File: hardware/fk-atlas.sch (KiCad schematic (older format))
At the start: 50 parts, among them J1 CONN-HDR-2x5, J2 MICRO-USB, J3 Conn_01x02, J4 Conn_01x09, Q1 2N7002LT1G, Q2 2N7002LT1G, Q3 2N7002LT1G, Q4 2N7002LT1G, Q5 2N7002LT1G, SW1 SPNO, U1 S25FL1xxK0XM, U2 ATSAMD21G18A-AU, U3 MCP1700T-3302E/MB, Y1 FC-135

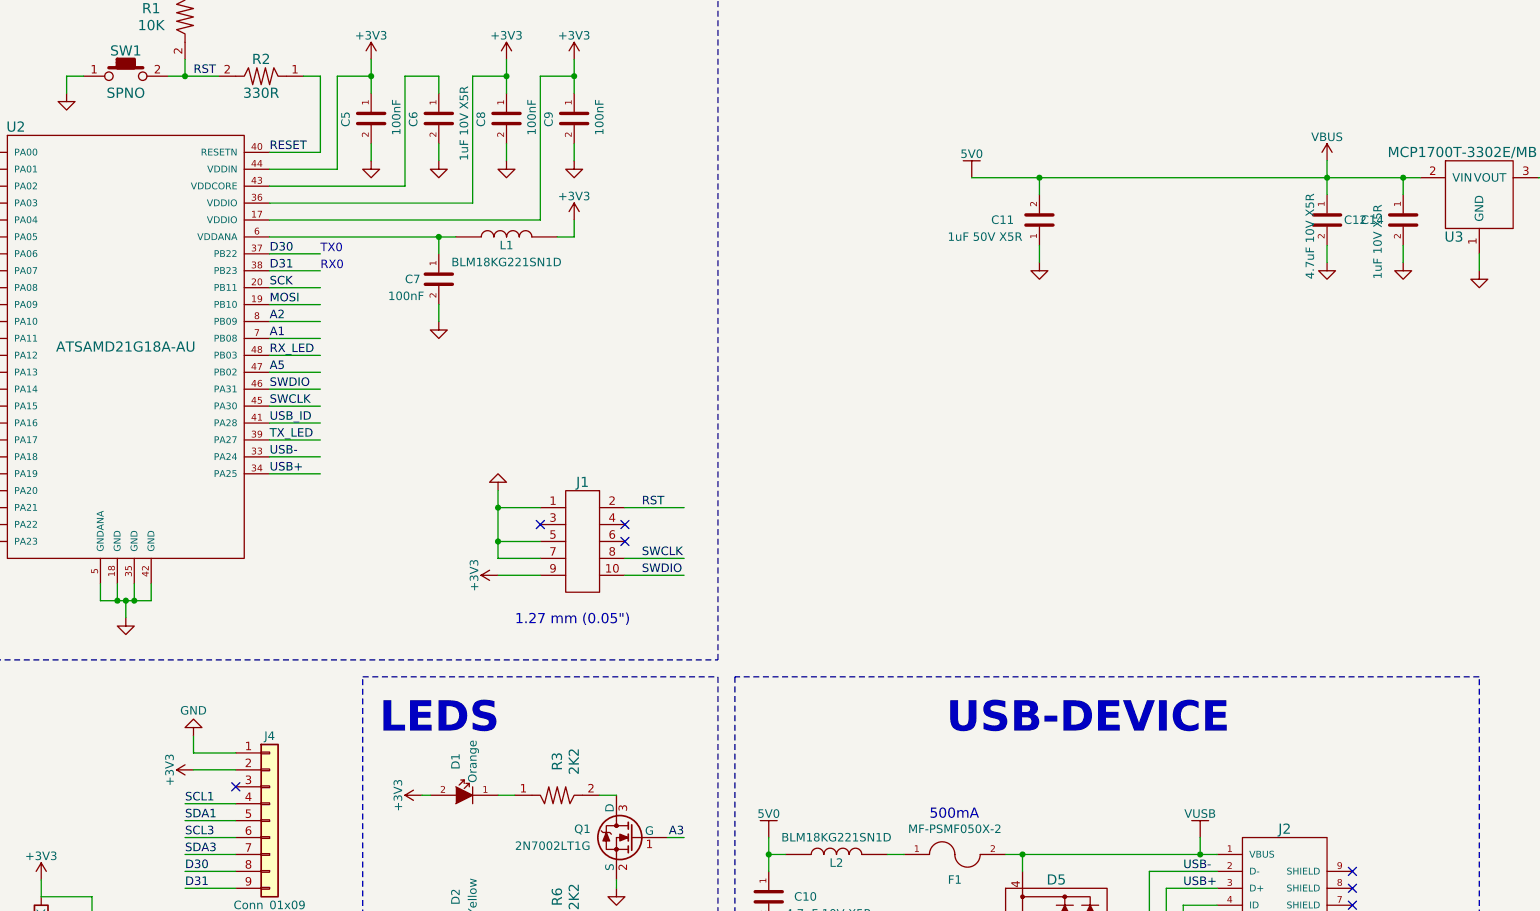
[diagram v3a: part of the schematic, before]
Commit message: Adding a Vin so we can provide an unregulated voltage.
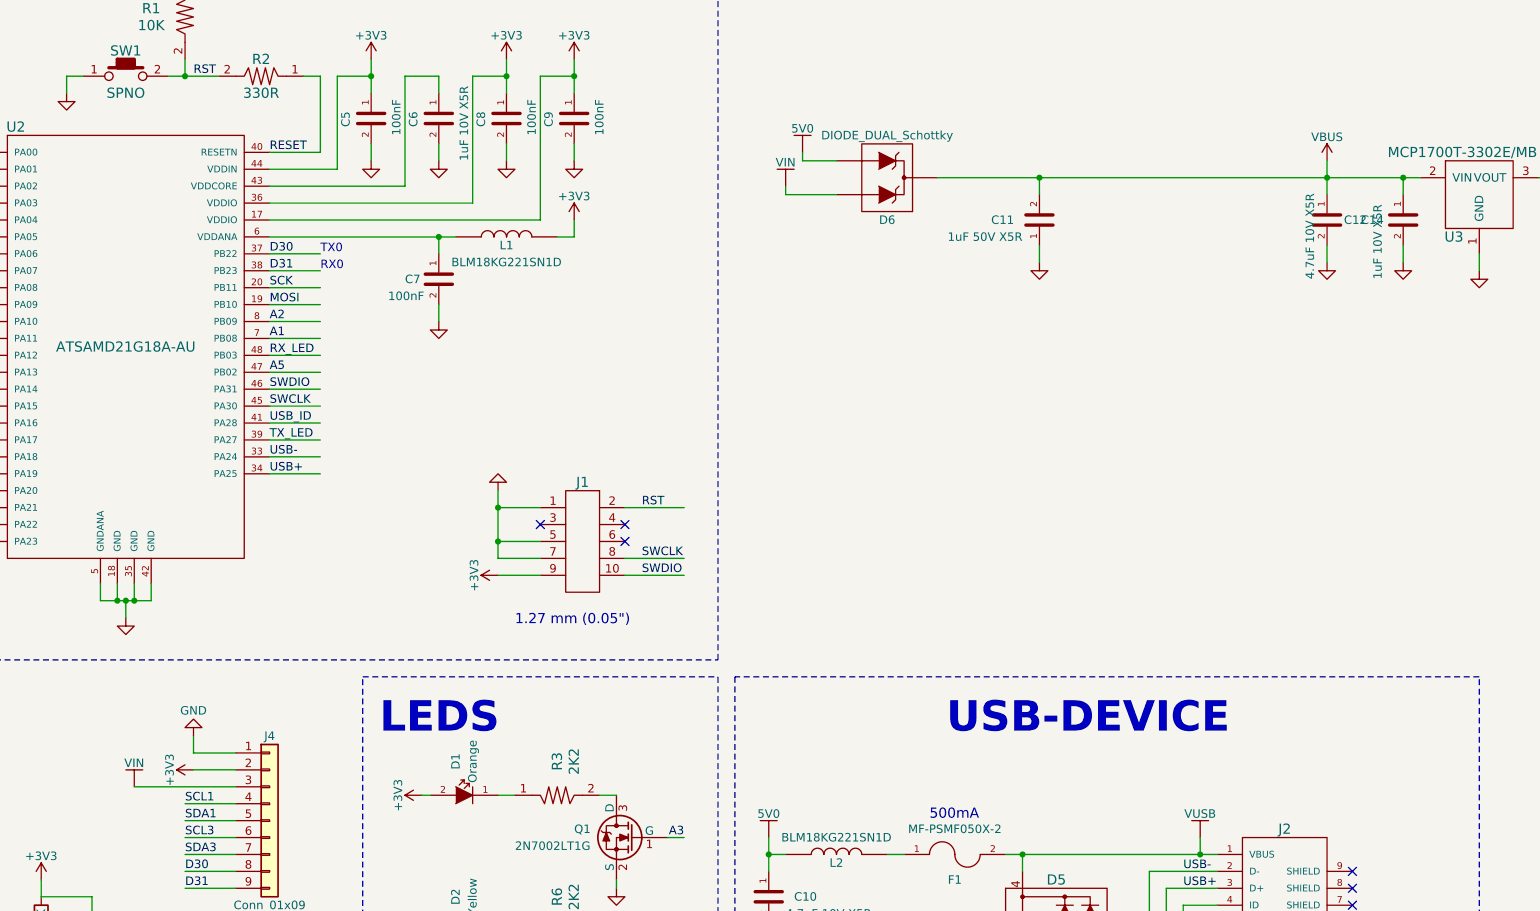
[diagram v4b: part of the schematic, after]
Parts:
- added D6: DIODE_DUAL_Schottky, RocketScreamKicadLibrary:SOT-1016, symbol DIODE_DUAL_Schottky
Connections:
- net labels added: VIN
- wire segments 218 -> 223
- no-connect marks 7 -> 6
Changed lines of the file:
@@
 L 5V0 #PWR024
 U 1 1 59A0A7FA
-P 8700 2250
-F 0 "#PWR024" H 8700 2100 50  0001 C CNN
-F 1 "5V0" H 8700 2390 50  0000 C CNN
-F 2 "" H 8700 2250 60  0000 C CNN
-F 3 "" H 8700 2250 60  0000 C CNN
-	1    8700 2250
-	1    0    0    -1
-$EndComp
-$Comp
-L 5V0 #PWR025
-U 1 1 59A0A7FB
-P 7500 6150
-F 0 "#PWR025" H 7500 6000 50  0001 C CNN
-F 1 "5V0" H 7500 6290 50  0000 C CNN
-F 2 "" H 7500 6150 60  0000 C CNN
-F 3 "" H 7500 6150 60  0000 C CNN
-	1    7500 6150
+P 7700 2100
+F 0 "#PWR024" H 7700 1950 50  0001 C CNN
+F 1 "5V0" H 7700 2240 50  0000 C CNN
+F 2 "" H 7700 2100 60  0000 C CNN
+F 3 "" H 7700 2100 60  0000 C CNN
+	1    7700 2100
 	1    0    0    -1
 $EndComp
@@
 $EndComp
 $Comp
-L GND #PWR026
+L GND #PWR025
 U 1 1 59A0A82D
 P 6600 8050
-F 0 "#PWR026" H 6600 7800 50  0001 C CNN
+F 0 "#PWR025" H 6600 7800 50  0001 C CNN
 F 1 "GND" H 6600 7900 50  0001 C CNN
 F 2 "" H 6600 8050 60  0000 C CNN
@@
 $EndComp
 $Comp
-L GND #PWR027
+L GND #PWR026
 U 1 1 59A0A836
 P 6600 7250
-F 0 "#PWR027" H 6600 7000 50  0001 C CNN
+F 0 "#PWR026" H 6600 7000 50  0001 C CNN
 F 1 "GND" H 6600 7100 50  0001 C CNN
 F 2 "" H 6600 7250 60  0000 C CNN
@@
 $EndComp
 $Comp
-L GND #PWR028
+L GND #PWR027
 U 1 1 59A0A837
 P 6600 6450
-F 0 "#PWR028" H 6600 6200 50  0001 C CNN
+F 0 "#PWR027" H 6600 6200 50  0001 C CNN
 F 1 "GND" H 6600 6300 50  0001 C CNN
 F 2 "" H 6600 6450 60  0000 C CNN
@@
 $EndComp
 $Comp
-L VBUS #PWR029
+L VBUS #PWR028
 U 1 1 59A0A7BF
 P 10800 2150
-F 0 "#PWR029" H 10800 2000 50  0001 C CNN
+F 0 "#PWR028" H 10800 2000 50  0001 C CNN
 F 1 "VBUS" H 10800 2290 50  0000 C CNN
 F 2 "" H 10800 2150 60  0000 C CNN
@@
 $EndComp
 $Comp
-L GND #PWR030
+L GND #PWR029
 U 1 1 59A0A7BD
 P 10800 2750
-F 0 "#PWR030" H 10800 2500 50  0001 C CNN
+F 0 "#PWR029" H 10800 2500 50  0001 C CNN
 F 1 "GND" H 10800 2600 50  0001 C CNN
 F 2 "" H 10800 2750 60  0000 C CNN
@@
 $EndComp
 $Comp
-L +3V3 #PWR031
+L +3V3 #PWR030
 U 1 1 59A1B0FE
 P 12150 2150
-F 0 "#PWR031" H 12150 2000 50  0001 C CNN
+F 0 "#PWR030" H 12150 2000 50  0001 C CNN
 F 1 "+3V3" H 12150 2290 50  0000 C CNN
 F 2 "" H 12150 2150 50  0000 C CNN
@@
 $EndComp
 $Comp
-L +3V3 #PWR032
+L +3V3 #PWR031
 U 1 1 59A1EC58
 P 6350 1550
-F 0 "#PWR032" H 6350 1400 50  0001 C CNN
+F 0 "#PWR031" H 6350 1400 50  0001 C CNN
 F 1 "+3V3" H 6350 1690 50  0000 C CNN
 F 2 "" H 6350 1550 50  0000 C CNN
@@
 $EndComp
 $Comp
-L +3V3 #PWR033
+L +3V3 #PWR032
 U 1 1 59A1F07B
 P 5950 1550
-F 0 "#PWR033" H 5950 1400 50  0001 C CNN
+F 0 "#PWR032" H 5950 1400 50  0001 C CNN
 F 1 "+3V3" H 5950 1690 50  0000 C CNN
 F 2 "" H 5950 1550 50  0000 C CNN
@@
 $EndComp
 $Comp
-L +3V3 #PWR034
+L +3V3 #PWR033
 U 1 1 59A1F185
 P 5150 1550
-F 0 "#PWR034" H 5150 1400 50  0001 C CNN
+F 0 "#PWR033" H 5150 1400 50  0001 C CNN
 F 1 "+3V3" H 5150 1690 50  0000 C CNN
 F 2 "" H 5150 1550 50  0000 C CNN
@@
 $EndComp
 $Comp
-L +3V3 #PWR035
+L +3V3 #PWR034
 U 1 1 59A1F434
 P 4050 950
-F 0 "#PWR035" H 4050 800 50  0001 C CNN
+F 0 "#PWR034" H 4050 800 50  0001 C CNN
 F 1 "+3V3" H 4050 1090 50  0000 C CNN
 F 2 "" H 4050 950 50  0000 C CNN
@@
 $EndComp
 $Comp
-L +3V3 #PWR036
+L +3V3 #PWR035
 U 1 1 59A2074B
 P 5900 4600
-F 0 "#PWR036" H 5900 4450 50  0001 C CNN
+F 0 "#PWR035" H 5900 4450 50  0001 C CNN
 F 1 "+3V3" H 5900 4740 50  0000 C CNN
 F 2 "" H 5900 4600 50  0000 C CNN
@@
 $EndComp
 $Comp
-L +3V3 #PWR037
+L +3V3 #PWR036
 U 1 1 59A229FA
 P 5450 5900
-F 0 "#PWR037" H 5450 5750 50  0001 C CNN
+F 0 "#PWR036" H 5450 5750 50  0001 C CNN
 F 1 "+3V3" H 5450 6040 50  0000 C CNN
 F 2 "" H 5450 5900 50  0000 C CNN
@@
 $EndComp
 $Comp
-L +3V3 #PWR038
+L +3V3 #PWR037
 U 1 1 59A22B04
 P 5450 6700
-F 0 "#PWR038" H 5450 6550 50  0001 C CNN
+F 0 "#PWR037" H 5450 6550 50  0001 C CNN
 F 1 "+3V3" H 5450 6840 50  0000 C CNN
 F 2 "" H 5450 6700 50  0000 C CNN
@@
 $EndComp
 $Comp
-L +3V3 #PWR039
+L +3V3 #PWR038
 U 1 1 59A22C0E
 P 5450 7500
-F 0 "#PWR039" H 5450 7350 50  0001 C CNN
+F 0 "#PWR038" H 5450 7350 50  0001 C CNN
 F 1 "+3V3" H 5450 7640 50  0000 C CNN
 F 2 "" H 5450 7500 50  0000 C CNN
@@
 $EndComp
 $Comp
-L +3V3 #PWR040
+L +3V3 #PWR039
 U 1 1 59A24411
 P 9250 7450
-F 0 "#PWR040" H 9250 7300 50  0001 C CNN
+F 0 "#PWR039" H 9250 7300 50  0001 C CNN
 F 1 "+3V3" H 9250 7590 50  0000 C CNN
 F 2 "" H 9250 7450 50  0000 C CNN
@@
 $EndComp
 $Comp
-L GND #PWR041
+L GND #PWR040
 U 1 1 59CC3FB7
 P 6600 9150
-F 0 "#PWR041" H 6600 8900 50  0001 C CNN
+F 0 "#PWR040" H 6600 8900 50  0001 C CNN
 F 1 "GND" H 6600 9000 50  0001 C CNN
 F 2 "" H 6600 9150 60  0000 C CNN
@@
 $EndComp
 $Comp
-L +3V3 #PWR042
+L +3V3 #PWR041
 U 1 1 59CC3FE1
 P 5450 8600
-F 0 "#PWR042" H 5450 8450 50  0001 C CNN
+F 0 "#PWR041" H 5450 8450 50  0001 C CNN
 F 1 "+3V3" H 5450 8740 50  0000 C CNN
 F 2 "" H 5450 8600 50  0000 C CNN
@@
 	10800 2150 10800 2350
 Wire Wire Line
-	8700 2250 11350 2250
+	8500 2250 11350 2250
 Wire Wire Line
 	9100 2350 9100 2250
@@
 Connection ~ 5900 4400
 Connection ~ 5900 4200
-NoConn ~ 4350 5850
 NoConn ~ 10950 6350
 NoConn ~ 10950 6450
@@
 NoConn ~ 6650 4400
 $Comp
-L +3V3 #PWR043
+L +3V3 #PWR042
 U 1 1 59FB8104
 P 6350 2500
-F 0 "#PWR043" H 6350 2350 50  0001 C CNN
+F 0 "#PWR042" H 6350 2350 50  0001 C CNN
 F 1 "+3V3" H 6350 2640 50  0000 C CNN
 F 2 "" H 6350 2500 50  0000 C CNN
@@
 $EndComp
 $Comp
-L GND #PWR044
+L GND #PWR043
 U 1 1 59FED5D9
 P 13750 6450
-F 0 "#PWR044" H 13750 6200 50  0001 C CNN
+F 0 "#PWR043" H 13750 6200 50  0001 C CNN
 F 1 "GND" H 13750 6300 50  0000 C CNN
 F 2 "" H 13750 6450 50  0000 C CNN
@@
 MISO
 $Comp
-L +3V3 #PWR045
+L +3V3 #PWR044
 U 1 1 5A1D08D0
 P 3600 9200
-F 0 "#PWR045" H 3600 9050 50  0001 C CNN
+F 0 "#PWR044" H 3600 9050 50  0001 C CNN
 F 1 "+3V3" H 3600 9340 50  0000 C CNN
 F 2 "" H 3600 9200 50  0000 C CNN
@@
 $EndComp
 $Comp
-L GND #PWR046
+L GND #PWR045
 U 1 1 5A1D1A01
 P 4250 9350
-F 0 "#PWR046" H 4250 9100 50  0001 C CNN
+F 0 "#PWR045" H 4250 9100 50  0001 C CNN
 F 1 "GND" H 4250 9200 50  0001 C CNN
 F 2 "" H 4250 9350 60  0000 C CNN
@@
 	3600 9450 3450 9450
 $Comp
-L +3V3 #PWR047
+L +3V3 #PWR046
 U 1 1 5A1D25E3
 P 1850 9200
-F 0 "#PWR047" H 1850 9050 50  0001 C CNN
+F 0 "#PWR046" H 1850 9050 50  0001 C CNN
 F 1 "+3V3" H 1850 9340 50  0000 C CNN
 F 2 "" H 1850 9200 50  0000 C CNN
@@
 $EndComp
 $Comp
-L GND #PWR048
+L GND #PWR047
 U 1 1 5A1D26FC
 P 1850 9850
-F 0 "#PWR048" H 1850 9600 50  0001 C CNN
+F 0 "#PWR047" H 1850 9600 50  0001 C CNN
 F 1 "GND" H 1850 9700 50  0001 C CNN
 F 2 "" H 1850 9850 60  0000 C CNN
@@
 FLASH_CS
 $Comp
-L GND #PWR049
+L GND #PWR048
 U 1 1 5A3A71A5
 P 13100 6450
-F 0 "#PWR049" H 13100 6200 50  0001 C CNN
+F 0 "#PWR048" H 13100 6200 50  0001 C CNN
 F 1 "GND" H 13100 6300 50  0000 C CNN
 F 2 "" H 13100 6450 50  0000 C CNN
@@
 Connection ~ 13100 4900
 $Comp
-L +3V3 #PWR050
+L +3V3 #PWR049
 U 1 1 5A3AC7A1
 P 13850 950
-F 0 "#PWR050" H 13850 800 50  0001 C CNN
+F 0 "#PWR049" H 13850 800 50  0001 C CNN
 F 1 "+3V3" H 13850 1090 50  0000 C CNN
 F 2 "" H 13850 950 50  0000 C CNN
@@
 $EndComp
 $Comp
-L +3V3 #PWR051
+L +3V3 #PWR050
 U 1 1 5A3AC928
 P 13850 1900
-F 0 "#PWR051" H 13850 1750 50  0001 C CNN
+F 0 "#PWR050" H 13850 1750 50  0001 C CNN
 F 1 "+3V3" H 13850 2040 50  0000 C CNN
 F 2 "" H 13850 1900 50  0000 C CNN
@@
 $EndComp
 $Comp
-L +3V3 #PWR052
+L +3V3 #PWR051
 U 1 1 5A3AD423
 P 13850 2850
-F 0 "#PWR052" H 13850 2700 50  0001 C CNN
+F 0 "#PWR051" H 13850 2700 50  0001 C CNN
 F 1 "+3V3" H 13850 2990 50  0000 C CNN
 F 2 "" H 13850 2850 50  0000 C CNN
@@
 $EndComp
 $Comp
-L +3V3 #PWR053
+L +3V3 #PWR052
 U 1 1 5A3AD5AA
 P 13850 3800
-F 0 "#PWR053" H 13850 3650 50  0001 C CNN
+F 0 "#PWR052" H 13850 3650 50  0001 C CNN
 F 1 "+3V3" H 13850 3940 50  0000 C CNN
 F 2 "" H 13850 3800 50  0000 C CNN
@@
 $EndComp
 $Comp
-L +3V3 #PWR054
+L +3V3 #PWR053
 U 1 1 5A3AE7F3
 P 13850 4750
-F 0 "#PWR054" H 13850 4600 50  0001 C CNN
+F 0 "#PWR053" H 13850 4600 50  0001 C CNN
 F 1 "+3V3" H 13850 4890 50  0000 C CNN
 F 2 "" H 13850 4750 50  0000 C CNN
@@
 	13850 1000 13850 950
 $Comp
-L GND #PWR055
+L GND #PWR054
 U 1 1 5A3B34F5
 P 12550 5500
-F 0 "#PWR055" H 12550 5250 50  0001 C CNN
+F 0 "#PWR054" H 12550 5250 50  0001 C CNN
 F 1 "GND" H 12550 5350 50  0000 C CNN
 F 2 "" H 12550 5500 50  0000 C CNN
@@
 Text Label 2400 3600 0    50   ~ 0
 FLASH_CS
+Wire Wire Line
+	4050 6350 4350 6350
+Wire Wire Line
+	4050 6450 4350 6450
+Text Label 4050 6450 0    50   ~ 0
+D31
+Text Label 4050 6350 0    50   ~ 0
+D30
+$Comp
+L 5V0 #PWR055
+U 1 1 59A0A7FB
+P 7500 6150
+F 0 "#PWR055" H 7500 6000 50  0001 C CNN
+F 1 "5V0" H 7500 6290 50  0000 C CNN
+F 2 "" H 7500 6150 60  0000 C CNN
+F 3 "" H 7500 6150 60  0000 C CNN
+	1    7500 6150
+	1    0    0    -1
+$EndComp
+$Comp
+L DIODE_DUAL_Schottky D6
+U 1 1 5A587855
+P 8200 2250
+F 0 "D6" H 8200 2500 50  0000 C CNN
+F 1 "DIODE_DUAL_Schottky" H 8200 2000 50  0000 C CNN
+F 2 "RocketScreamKicadLibrary:SOT-1016" H 8200 1900 60  0001 C CNN
+F 3 "" H 8200 2350 60  0000 C CNN
+	1    8200 2250
+	-1   0    0    1
+$EndComp
+$Comp
+L VIN #PWR056
+U 1 1 5A587C10
+P 7600 2300
+F 0 "#PWR056" H 7600 2150 50  0001 C CNN
+F 1 "VIN" H 7600 2440 50  0000 C CNN
+F 2 "" H 7600 2300 60  0000 C CNN
+F 3 "" H 7600 2300 60  0000 C CNN
+	1    7600 2300
+	1    0    0    -1
+$EndComp
+Wire Wire Line
+	7700 2100 7700 2150
+Wire Wire Line
+	7700 2150 7900 2150
+Wire Wire Line
+	7900 2350 7600 2350
+Wire Wire Line
+	7600 2350 7600 2300
+$Comp
+L VIN #PWR?
+U 1 1 5A58936C
+P 3750 5850
+F 0 "#PWR?" H 3750 5700 50  0001 C CNN
+F 1 "VIN" H 3750 5990 50  0000 C CNN
+F 2 "" H 3750 5850 60  0000 C CNN
+F 3 "" H 3750 5850 60  0000 C CNN
+	1    3750 5850
+	1    0    0    -1
+$EndComp
 $Comp
 L Conn_01x09 J4
@@
 $EndComp
 Wire Wire Line
-	4050 6350 4350 6350
-Wire Wire Line
-	4050 6450 4350 6450
-Text Label 4050 6450 0    50   ~ 0
-D31
-Text Label 4050 6350 0    50   ~ 0
-D30
+	4350 5850 3750 5850
 $EndSCHEMATC

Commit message: Add LED labels, make room for mounting in one corner.
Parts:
- D1, D2, D3, D4: footprint LEDs:LED_0603_HandSoldering -> RocketScreamKicadLibrary:LED-0603
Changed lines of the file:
@@
 F 0 "D1" V 5750 5700 50  0000 C CNN
 F 1 "Orange" V 5650 5700 50  0000 C CNN
-F 2 "LEDs:LED_0603_HandSoldering" H 5700 5650 60  0001 C CNN
+F 2 "RocketScreamKicadLibrary:LED-0603" H 5700 5650 60  0001 C CNN
 F 3 "" H 5700 5900 60  0000 C CNN
 F 4 "0" H 5750 5800 50  0001 C CNN "price"
@@
 F 0 "D2" V 5750 6500 50  0000 C CNN
 F 1 "Yellow" V 5650 6500 50  0000 C CNN
-F 2 "LEDs:LED_0603_HandSoldering" H 5700 6450 60  0001 C CNN
+F 2 "RocketScreamKicadLibrary:LED-0603" H 5700 6450 60  0001 C CNN
 F 3 "" H 5700 6700 60  0000 C CNN
 F 4 "0" H 5750 6600 50  0001 C CNN "price"
@@
 F 0 "D3" V 5750 7300 50  0000 C CNN
 F 1 "Blue" V 5650 7300 50  0000 C CNN
-F 2 "LEDs:LED_0603_HandSoldering" H 5700 7250 60  0001 C CNN
+F 2 "RocketScreamKicadLibrary:LED-0603" H 5700 7250 60  0001 C CNN
 F 3 "" H 5700 7500 60  0000 C CNN
 F 4 "0" H 5750 7400 50  0001 C CNN "price"
@@
 F 0 "D4" V 5750 8400 50  0000 C CNN
 F 1 "Orange" V 5650 8400 50  0000 C CNN
-F 2 "LEDs:LED_0603_HandSoldering" H 5700 8350 60  0001 C CNN
+F 2 "RocketScreamKicadLibrary:LED-0603" H 5700 8350 60  0001 C CNN
 F 3 "" H 5700 8600 60  0000 C CNN
 F 4 "0" H 5750 8500 50  0001 C CNN "price"
@@
 	7600 2350 7600 2300
 $Comp
-L VIN #PWR?
+L VIN #PWR057
 U 1 1 5A58936C
 P 3750 5850
-F 0 "#PWR?" H 3750 5700 50  0001 C CNN
+F 0 "#PWR057" H 3750 5700 50  0001 C CNN
 F 1 "VIN" H 3750 5990 50  0000 C CNN
 F 2 "" H 3750 5850 60  0000 C CNN

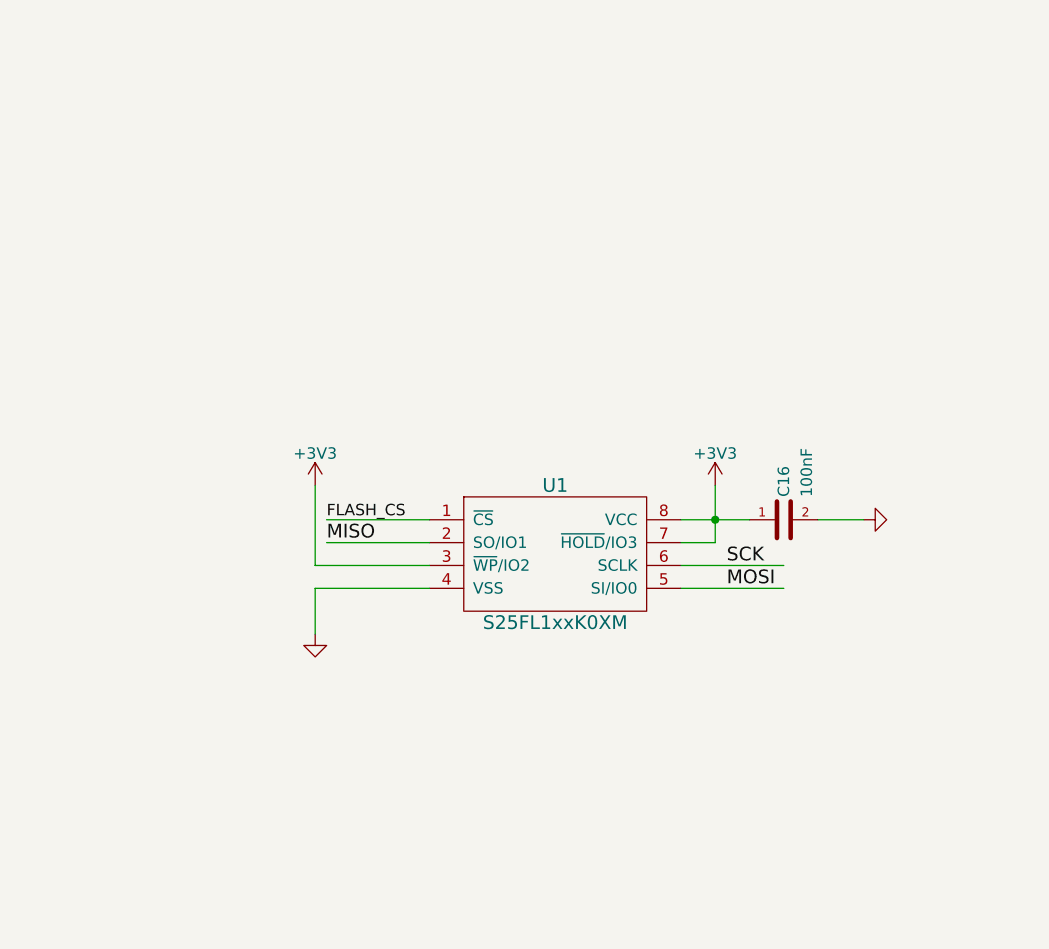
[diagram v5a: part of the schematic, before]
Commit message: Adding mounting holes for Atlas.
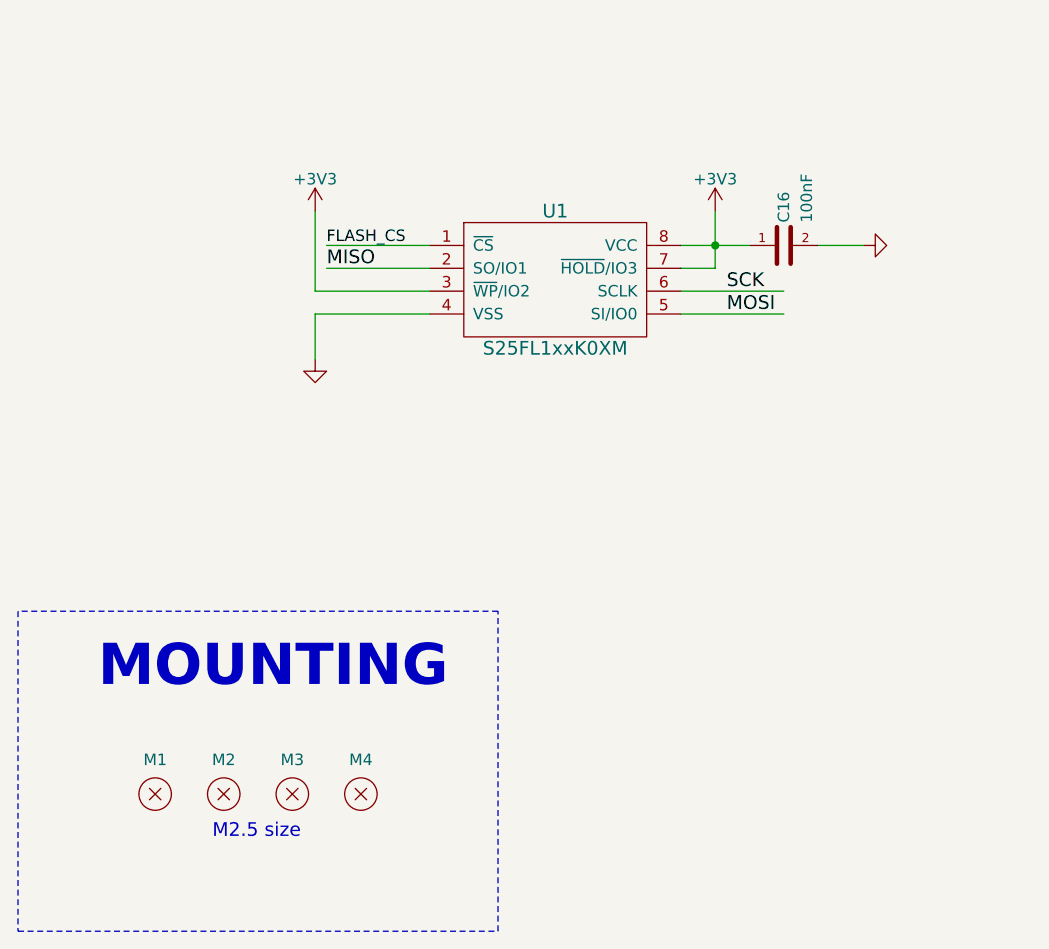
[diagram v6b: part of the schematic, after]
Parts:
- added M1, M2, M3, M4: MOUNT_HOLE, RocketScreamKicadLibrary:HOLE_NPTH_2.2MM, symbol MOUNT_HOLE
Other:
- note added: "M2.5 size"
- note added: "MOUNTING"
- moved on the sheet: C16, U1
